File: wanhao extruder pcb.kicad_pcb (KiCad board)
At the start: 2 copper layers, 36.2 x 27.4 mm, 11 parts, among them J1 Conn_02x10_Counter_Clockwise, T0 Conn_01x02

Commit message: Changed text label for extruder board
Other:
- board text added: "Mk2 BL V1.1"
- board text removed: "Plus & D6 BL V1.1"
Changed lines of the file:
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@@
   (page A4)
   (layers
-    (0 F.Cu signal)
-    (31 B.Cu signal)
+    (0 F.Cu signal hide)
+    (31 B.Cu signal hide)
     (32 B.Adhes user hide)
     (33 F.Adhes user hide)
@@
     (35 F.Paste user hide)
     (36 B.SilkS user hide)
-    (37 F.SilkS user hide)
+    (37 F.SilkS user)
     (38 B.Mask user hide)
     (39 F.Mask user hide)
@@
     (effects (font (size 1 1) (thickness 0.15)) (justify mirror))
   )
-  (gr_text "Plus & D6 BL V1.1" (at 188.18873 89.160242) (layer F.SilkS)
+  (gr_text "Mk2 BL V1.1" (at 191.287979 89.160242) (layer F.SilkS)
     (effects (font (size 1 1) (thickness 0.15)))
   )

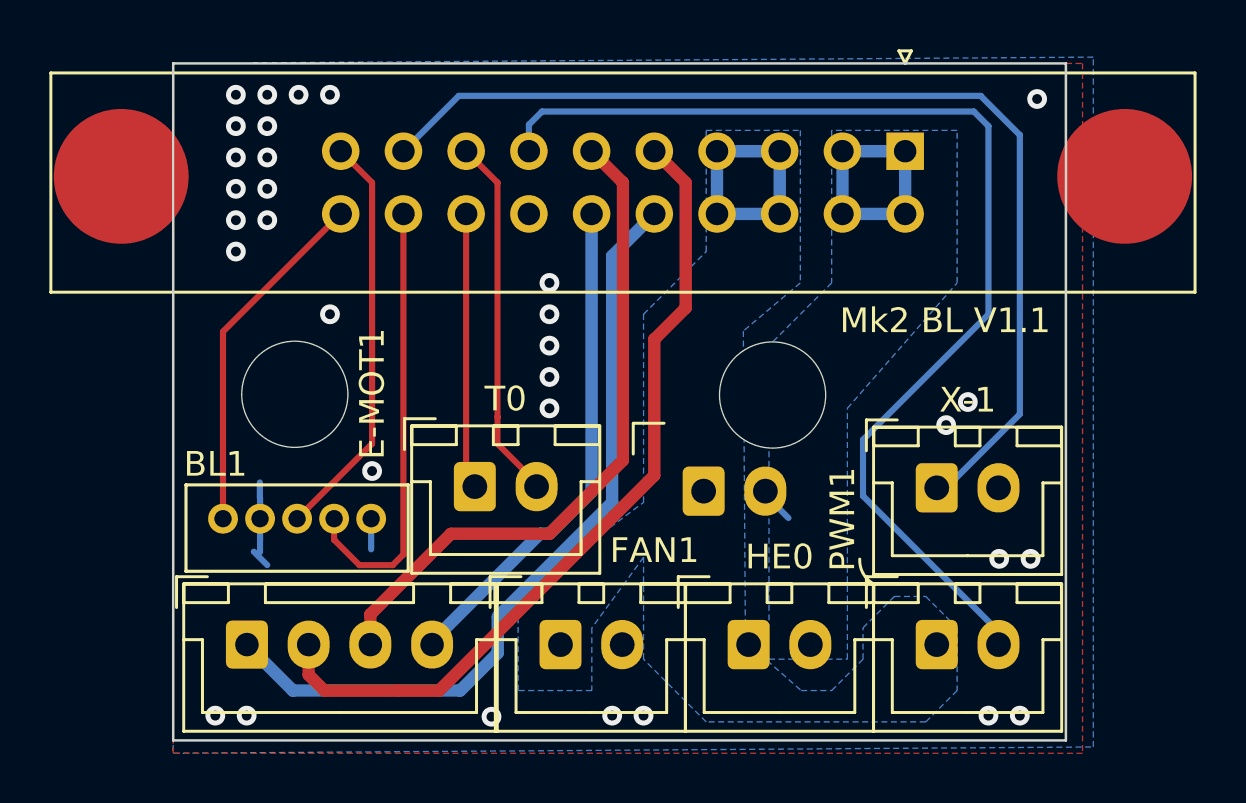
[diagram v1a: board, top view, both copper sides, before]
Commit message: Increased sizing of heater trace fills
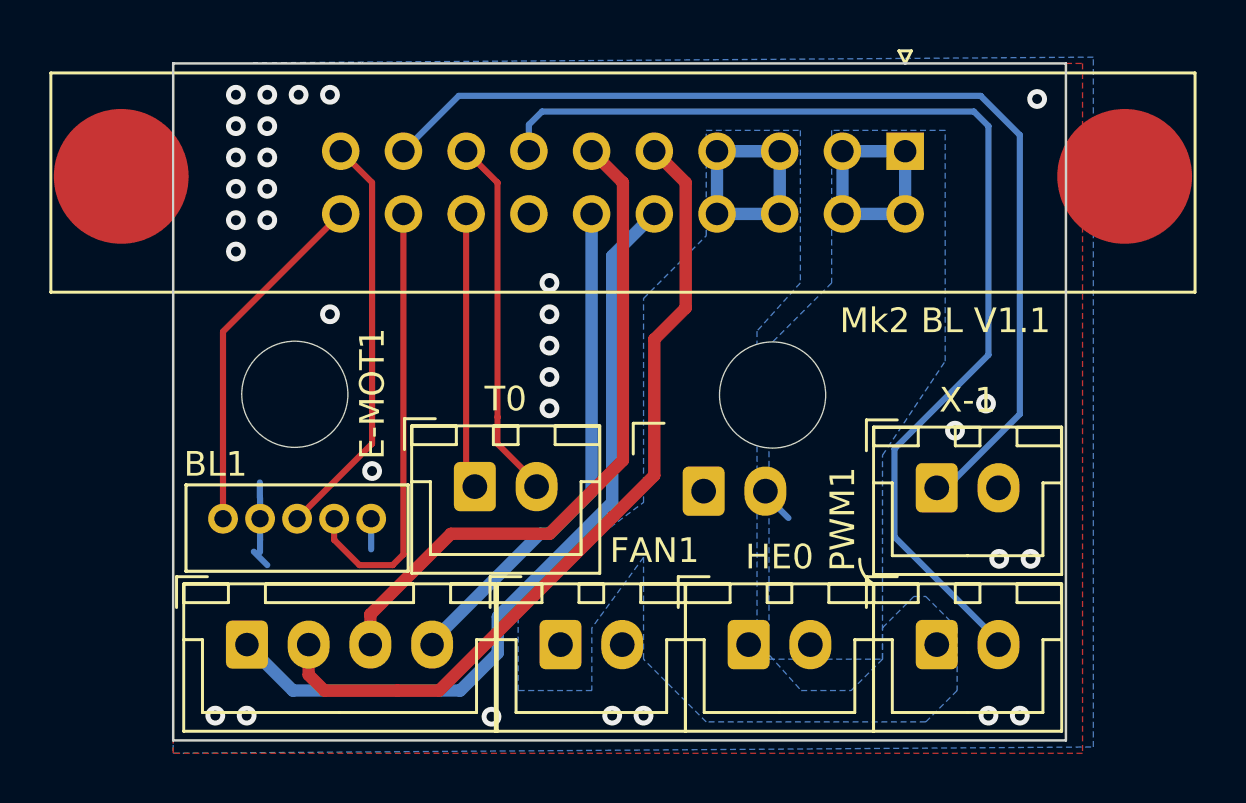
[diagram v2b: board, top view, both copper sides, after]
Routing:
- net /PWMFAN-GND: track 45.7 -> 44.6 mm
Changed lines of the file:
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@@
     (thickness 1.6)
     (drawings 25)
-    (tracks 112)
+    (tracks 113)
     (zones 0)
     (modules 11)
@@
   (page A4)
   (layers
-    (0 F.Cu signal hide)
-    (31 B.Cu signal hide)
+    (0 F.Cu signal)
+    (31 B.Cu signal)
     (32 B.Adhes user hide)
     (33 F.Adhes user hide)
@@
     (42 Eco1.User user hide)
     (43 Eco2.User user hide)
-    (44 Edge.Cuts user hide)
+    (44 Edge.Cuts user)
     (45 Margin user hide)
     (46 B.CrtYd user hide)
@@
     (pad_to_mask_clearance 0.051)
     (solder_mask_min_width 0.25)
-    (aux_axis_origin 196.176334 106.15985)
+    (aux_axis_origin 160.02 106.15985)
     (grid_origin 172.237979 95.880146)
     (visible_elements 7FFFFFFF)
@@
   (via (at 194.745612 98.805892) (size 0.8) (drill 0.4) (layers F.Cu B.Cu) (net 1))
   (via (at 193.475612 98.805892) (size 0.8) (drill 0.4) (layers F.Cu B.Cu) (net 1))
-  (via (at 192.205612 92.455892) (size 0.8) (drill 0.4) (layers F.Cu B.Cu) (net 1))
   (via (at 161.725612 105.155892) (size 0.8) (drill 0.4) (layers F.Cu B.Cu) (net 1))
   (via (at 162.995612 105.155892) (size 0.8) (drill 0.4) (layers F.Cu B.Cu) (net 1))
@@
   (via (at 168.075612 95.25) (size 0.8) (drill 0.4) (layers F.Cu B.Cu) (net 1))
   (segment (start 168.037979 97.180146) (end 168.037979 98.421168) (width 0.25) (layer B.Cu) (net 1))
-  (via (at 191.32685 93.389039) (size 0.8) (drill 0.4) (layers F.Cu B.Cu) (net 1))
   (via (at 172.91185 105.200039) (size 0.8) (drill 0.4) (layers F.Cu B.Cu) (net 1))
   (via (at 195.00985 80.181039) (size 0.8) (drill 0.4) (layers F.Cu B.Cu) (net 1))
+  (via (at 192.940614 92.517118) (size 0.8) (drill 0.4) (layers F.Cu B.Cu) (net 1))
+  (via (at 191.684414 93.614488) (size 0.8) (drill 0.4) (layers F.Cu B.Cu) (net 1))
   (segment (start 184.585612 82.295892) (end 184.585612 84.835892) (width 0.5) (layer B.Cu) (net 2))
   (segment (start 182.045612 82.295892) (end 184.585612 82.295892) (width 0.5) (layer B.Cu) (net 2))
@@
   (segment (start 173.155612 83.565892) (end 173.155612 93.071281) (width 0.25) (layer F.Cu) (net 9))
   (segment (start 193.82685 102.129039) (end 193.82685 102.279039) (width 0.25) (layer B.Cu) (net 10))
-  (segment (start 187.96 96.262189) (end 193.82685 102.129039) (width 0.25) (layer B.Cu) (net 10))
-  (segment (start 193.04 81.28) (end 193.04 88.9) (width 0.25) (layer B.Cu) (net 10))
-  (segment (start 193.04 88.9) (end 187.96 93.98) (width 0.25) (layer B.Cu) (net 10))
-  (segment (start 187.96 93.98) (end 187.96 96.262189) (width 0.25) (layer B.Cu) (net 10))
-  (segment (start 174.425612 81.22109) (end 174.957663 80.689039) (width 0.25) (layer B.Cu) (net 10))
-  (segment (start 174.425612 82.295892) (end 174.425612 81.22109) (width 0.25) (layer B.Cu) (net 10))
-  (segment (start 192.449039 80.689039) (end 193.04 81.28) (width 0.25) (layer B.Cu) (net 10))
-  (segment (start 174.957663 80.689039) (end 192.449039 80.689039) (width 0.25) (layer B.Cu) (net 10))
+  (segment (start 193.44585 102.279039) (end 193.44585 102.129039) (width 0.25) (layer B.Cu) (net 10))
+  (segment (start 193.44585 102.129039) (end 189.233021 97.91621) (width 0.25) (layer B.Cu) (net 10))
+  (segment (start 193.04 90.548502) (end 193.04 81.28) (width 0.25) (layer B.Cu) (net 10))
+  (segment (start 193.04 81.28) (end 192.449039 80.689039) (width 0.25) (layer B.Cu) (net 10))
+  (segment (start 189.233021 97.91621) (end 189.233021 94.355481) (width 0.25) (layer B.Cu) (net 10))
+  (segment (start 192.449039 80.689039) (end 174.957663 80.689039) (width 0.25) (layer B.Cu) (net 10))
+  (segment (start 174.957663 80.689039) (end 174.425612 81.22109) (width 0.25) (layer B.Cu) (net 10))
+  (segment (start 174.425612 81.22109) (end 174.425612 82.295892) (width 0.25) (layer B.Cu) (net 10))
+  (segment (start 189.233021 94.355481) (end 193.04 90.548502) (width 0.25) (layer B.Cu) (net 10))
   (segment (start 176.965612 96.084388) (end 176.965612 84.835892) (width 0.5) (layer B.Cu) (net 11))
   (segment (start 175.26 97.79) (end 176.965612 96.084388) (width 0.5) (layer B.Cu) (net 11))
@@
   (zone (net 3) (net_name /HEATGND) (layer B.Cu) (hatch edge 0.508)
     (priority 1)
-    (connect_pads (clearance 0.508))
+    (connect_pads (clearance 0.8))
     (min_thickness 0.254)
     (fill yes (arc_segments 32) (thermal_gap 0.508) (thermal_bridge_width 0.508))
     (polygon
       (pts
-        (xy 191.77 81.451039) (xy 186.69 81.451039) (xy 186.69 85.09) (xy 186.69 87.63) (xy 184.15 90.17)
-        (xy 184.15 102.87) (xy 187.325 102.87) (xy 187.325 92.71) (xy 191.77 87.63)
+        (xy 191.287979 81.451039) (xy 186.69 81.451039) (xy 186.69 85.09) (xy 186.69 87.63) (xy 184.15 90.17)
+        (xy 184.15 102.87) (xy 188.747979 102.87) (xy 188.747979 94.610146) (xy 191.287979 90.800146)
       )
     )
@@
   )
   (zone (net 2) (net_name /24V) (layer B.Cu) (hatch edge 0.508)
-    (priority 1)
-    (connect_pads (clearance 0.508))
+    (priority 2)
+    (connect_pads (clearance 0.8))
     (min_thickness 0.254)
     (fill yes (arc_segments 32) (thermal_gap 0.508) (thermal_bridge_width 0.508))
     (polygon
       (pts
-        (xy 185.42 87.63) (xy 183.111369 89.579039) (xy 183.19885 102.152039) (xy 185.453775 104.14) (xy 186.69 104.14)
-        (xy 187.96 102.87) (xy 187.96 101.6) (xy 189.23 100.33) (xy 190.5 100.33) (xy 191.77 101.6)
+        (xy 185.42 87.63) (xy 183.667979 89.579039) (xy 183.667979 102.152039) (xy 185.453775 104.14) (xy 187.477979 104.14)
+        (xy 188.747979 102.87) (xy 188.747979 101.6) (xy 190.017979 100.33) (xy 190.5 100.33) (xy 191.77 101.6)
         (xy 191.77 104.14) (xy 190.5 105.41) (xy 181.61 105.41) (xy 179.07 102.87) (xy 179.07 98.7425)
         (xy 176.97585 101.6) (xy 176.97585 104.14) (xy 173.99 104.14) (xy 173.99 100.33) (xy 179.07 96.52)
-        (xy 179.07 88.9) (xy 181.61 86.36) (xy 181.61 81.451039) (xy 185.42 81.451039)
+        (xy 179.07 88.260146) (xy 181.61 85.720146) (xy 181.61 81.451039) (xy 185.42 81.451039)
       )
     )

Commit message: Updates to extruder board
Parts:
- renumbered HE0 to HE0-0, HE0 to HE0-1
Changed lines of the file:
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@@
   (page A4)
   (layers
-    (0 F.Cu signal)
+    (0 F.Cu signal hide)
     (31 B.Cu signal)
     (32 B.Adhes user hide)
@@
     (34 B.Paste user hide)
     (35 F.Paste user hide)
-    (36 B.SilkS user hide)
+    (36 B.SilkS user)
     (37 F.SilkS user)
     (38 B.Mask user hide)
@@
     (solder_mask_min_width 0.25)
     (aux_axis_origin 160.02 106.15985)
-    (grid_origin 172.237979 95.880146)
     (visible_elements 7FFFFFFF)
     (pcbplotparams
@@
     (descr "JST XH series connector, B2B-XH-A (http://www.jst-mfg.com/product/pdf/eng/eXH.pdf), generated with kicad-footprint-generator")
     (tags "connector JST XH vertical")
-    (fp_text reference HE0 (at 1.25 -3.55) (layer F.SilkS) hide
+    (fp_text reference HE0-1 (at 1.25 -3.55) (layer F.SilkS) hide
       (effects (font (size 1 1) (thickness 0.15)))
     )
@@
     (descr "JST XH series connector, B2B-XH-A (http://www.jst-mfg.com/product/pdf/eng/eXH.pdf), generated with kicad-footprint-generator")
     (tags "connector JST XH vertical")
-    (fp_text reference HE0 (at 1.25 -3.55) (layer F.SilkS)
+    (fp_text reference HE0-0 (at 1.25 -3.55) (layer F.SilkS)
       (effects (font (size 1 1) (thickness 0.15)))
     )
@@
   (via (at 179.07 105.155892) (size 0.8) (drill 0.4) (layers F.Cu B.Cu) (net 1))
   (via (at 177.8 105.155892) (size 0.8) (drill 0.4) (layers F.Cu B.Cu) (net 1))
-  (segment (start 163.283979 98.513979) (end 163.83 99.06) (width 0.25) (layer B.Cu) (net 1))
   (via (at 194.745612 98.805892) (size 0.8) (drill 0.4) (layers F.Cu B.Cu) (net 1))
   (via (at 193.475612 98.805892) (size 0.8) (drill 0.4) (layers F.Cu B.Cu) (net 1))
   (via (at 161.725612 105.155892) (size 0.8) (drill 0.4) (layers F.Cu B.Cu) (net 1))
   (via (at 162.995612 105.155892) (size 0.8) (drill 0.4) (layers F.Cu B.Cu) (net 1))
-  (segment (start 163.537687 98.034622) (end 163.537687 98.53298) (width 0.25) (layer B.Cu) (net 1))
-  (segment (start 163.537979 97.180146) (end 163.537979 98.03433) (width 0.25) (layer B.Cu) (net 1))
-  (segment (start 163.537979 98.03433) (end 163.537687 98.034622) (width 0.25) (layer B.Cu) (net 1))
-  (segment (start 163.530437 96.31842) (end 163.530437 95.712853) (width 0.25) (layer B.Cu) (net 1))
-  (segment (start 163.537979 97.180146) (end 163.537979 96.325962) (width 0.25) (layer B.Cu) (net 1))
-  (segment (start 163.537979 96.325962) (end 163.530437 96.31842) (width 0.25) (layer B.Cu) (net 1))
   (via (at 168.075612 95.25) (size 0.8) (drill 0.4) (layers F.Cu B.Cu) (net 1))
-  (segment (start 168.037979 97.180146) (end 168.037979 98.421168) (width 0.25) (layer B.Cu) (net 1))
   (via (at 172.91185 105.200039) (size 0.8) (drill 0.4) (layers F.Cu B.Cu) (net 1))
   (via (at 195.00985 80.181039) (size 0.8) (drill 0.4) (layers F.Cu B.Cu) (net 1))
   (via (at 192.940614 92.517118) (size 0.8) (drill 0.4) (layers F.Cu B.Cu) (net 1))
   (via (at 191.684414 93.614488) (size 0.8) (drill 0.4) (layers F.Cu B.Cu) (net 1))
+  (segment (start 168.037979 97.180146) (end 168.037979 98.421168) (width 0.25) (layer B.Cu) (net 1))
+  (segment (start 163.537979 97.180146) (end 163.537979 96.325962) (width 0.25) (layer B.Cu) (net 1))
+  (segment (start 163.537979 97.180146) (end 163.537979 98.03433) (width 0.25) (layer B.Cu) (net 1))
+  (segment (start 163.537979 96.325962) (end 163.530437 96.31842) (width 0.25) (layer B.Cu) (net 1))
+  (segment (start 163.537979 98.03433) (end 163.537687 98.034622) (width 0.25) (layer B.Cu) (net 1))
+  (segment (start 163.283979 98.513979) (end 163.83 99.06) (width 0.25) (layer B.Cu) (net 1))
+  (segment (start 163.537687 98.034622) (end 163.537687 98.53298) (width 0.25) (layer B.Cu) (net 1))
+  (segment (start 163.530437 96.31842) (end 163.530437 95.712853) (width 0.25) (layer B.Cu) (net 1))
   (segment (start 184.585612 82.295892) (end 184.585612 84.835892) (width 0.5) (layer B.Cu) (net 2))
   (segment (start 182.045612 82.295892) (end 184.585612 82.295892) (width 0.5) (layer B.Cu) (net 2))
